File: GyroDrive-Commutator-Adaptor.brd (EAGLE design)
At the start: 108 x 76.2 mm, 16 parts, among them U1 HALL, U2 PCA9517, U3 5V, U4 2.5V, U5 INA2141U, X1 NORCOMP-DB25-SMD-MALE

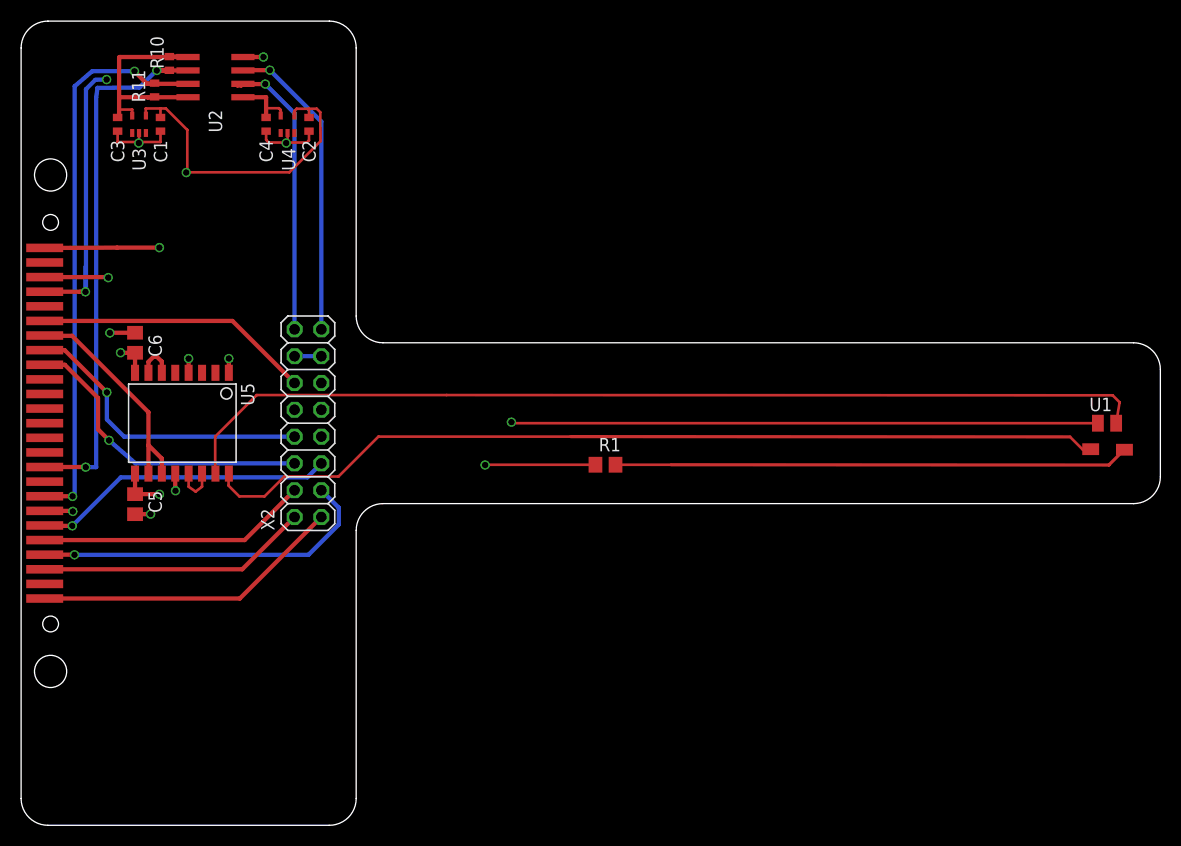
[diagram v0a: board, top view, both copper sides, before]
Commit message: narrower board - removed empty space
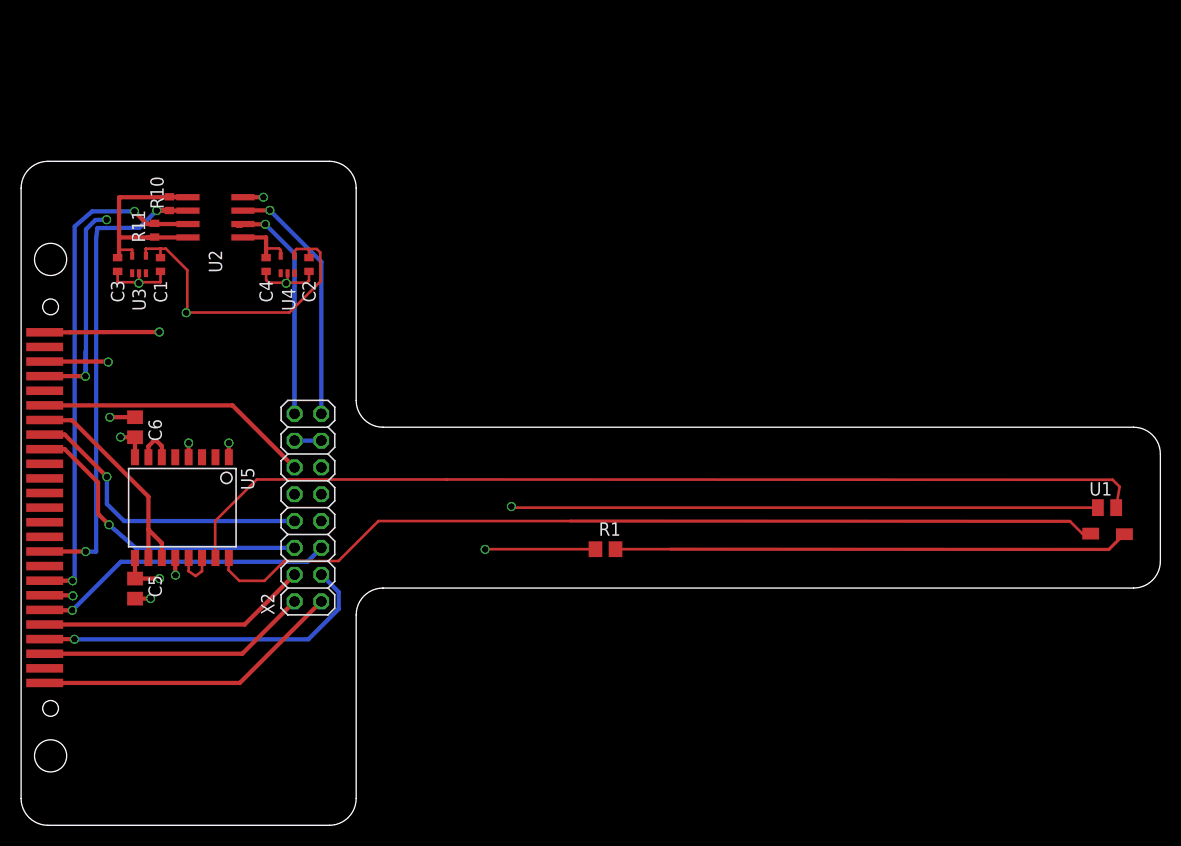
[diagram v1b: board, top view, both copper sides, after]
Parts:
- moved C1 13.3 mm to (13.2, 53.1)
- moved C2 13.3 mm to (27.3, 53.1)
- moved C3 13.3 mm to (9.14, 53.1)
- moved C4 13.3 mm to (23.2, 53.1)
- moved R10 13.3 mm to (14.0, 58.9)
- moved R11 13.3 mm to (12.6, 56.4)
- moved U2 13.3 mm to (18.4, 57.6)
- moved U3 13.3 mm to (11.2, 53.1)
- moved U4 13.3 mm to (25.2, 53.1)
- moved C5 8.00 mm to (10.8, 22.4)
- moved U1 8.00 mm to (102.9, 30.1)
- moved U5 8.00 mm to (15.2, 30.1)
- moved X1 8.00 mm to (0.00, 30.1)
- moved X2 8.00 mm to (27.2, 30.1)
- moved C6 8.00 mm to (10.8, 37.7)
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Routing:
- net SDA_RIG: track 51.3 -> 46.0 mm
- net SDA_BIRD: track 29.1 -> 23.9 mm
- net SCL_RIG: track 54.1 -> 48.8 mm
- net DGND: track 49.5 -> 44.2 mm
- net SCL_BIRD: track 27.7 -> 22.4 mm
- net V+: track 146.0 -> 144.1 mm
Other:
- board size 108 x 76.2 mm -> 108 x 62.9 mm
